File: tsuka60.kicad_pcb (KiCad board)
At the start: 2 copper layers, 285 x 95.1 mm, 175 parts, among them SW1 SW_Push, U1 ATmega32U4-AU, Y1 Resonator_Small

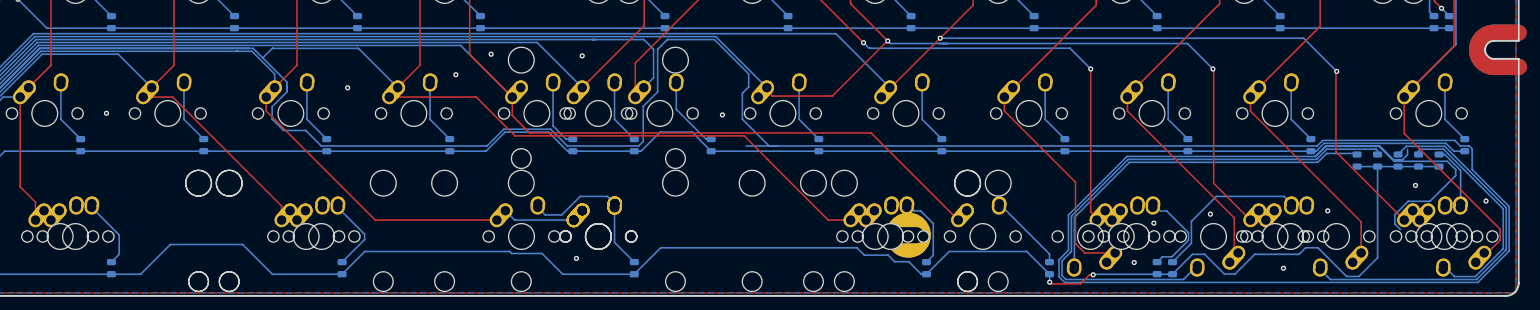
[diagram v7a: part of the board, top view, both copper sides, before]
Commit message: fixed broken trace
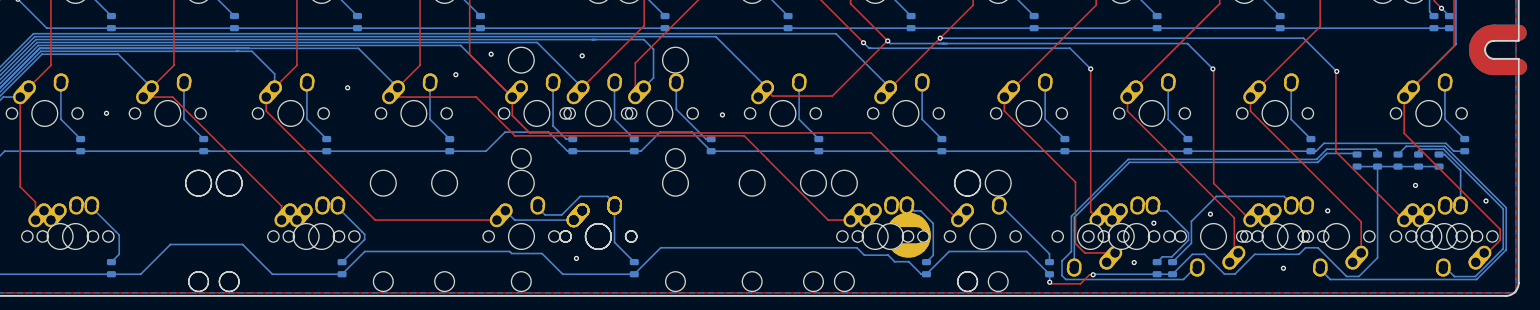
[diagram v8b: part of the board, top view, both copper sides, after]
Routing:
- net Col5: track 759.1 -> 325.0 mm
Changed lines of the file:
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@@
     (thickness 1.6)
     (drawings 1)
-    (tracks 1124)
+    (tracks 1058)
     (zones 0)
     (modules 175)
@@
   (segment (start 209.70875 171.14125) (end 206.25625 174.59375) (width 0.254) (layer F.Cu) (net 84))
   (segment (start 209.70875 157.00375) (end 209.70875 171.14125) (width 0.254) (layer F.Cu) (net 84))
-  (segment (start 139.745453 187.52206) (end 141.40956 185.857953) (width 0.254) (layer B.Cu) (net 84))
-  (segment (start 127.081547 187.52206) (end 139.745453 187.52206) (width 0.254) (layer B.Cu) (net 84))
-  (segment (start 141.40956 185.857953) (end 141.40956 177.90377) (width 0.254) (layer B.Cu) (net 84))
-  (segment (start 141.40956 177.90377) (end 150.80028 168.51305) (width 0.254) (layer B.Cu) (net 84))
-  (segment (start 200.17555 168.51305) (end 206.25625 174.59375) (width 0.254) (layer B.Cu) (net 84))
   (segment (start 224.417548 182.06401) (end 218.407288 176.05375) (width 0.254) (layer F.Cu) (net 84))
   (segment (start 259.91501 182.06401) (end 224.417548 182.06401) (width 0.254) (layer F.Cu) (net 84))
@@
   (segment (start 139.745454 187.52206) (end 141.40956 185.857954) (width 0.254) (layer B.Cu) (net 84))
   (segment (start 118.123 177.94) (end 118.123 180.734) (width 0.254) (layer B.Cu) (net 84))
-  (segment (start 189.103 175.006) (end 189.103 173.736) (width 0.254) (layer B.Cu) (net 84))
-  (segment (start 189.103 174.341538) (end 189.103 175.006) (width 0.254) (layer B.Cu) (net 84))
-  (segment (start 150.80028 168.51305) (end 183.88005 168.51305) (width 0.254) (layer B.Cu) (net 84))
-  (segment (start 186.95995 168.51305) (end 186.83295 168.51305) (width 0.254) (layer B.Cu) (net 84))
-  (segment (start 185.3565 169.9895) (end 183.88005 168.51305) (width 0.254) (layer B.Cu) (net 84))
-  (segment (start 186.83295 168.51305) (end 185.3565 169.9895) (width 0.254) (layer B.Cu) (net 84))
-  (segment (start 189.103 173.736) (end 185.3565 169.9895) (width 0.254) (layer B.Cu) (net 84))
-  (segment (start 186.95995 168.51305) (end 200.17555 168.51305) (width 0.254) (layer B.Cu) (net 84))
-  (segment (start 264.94101 183.62299) (end 260.20399 183.62299) (width 0.254) (layer B.Cu) (net 84))
-  (segment (start 349.931948 183.67523) (end 348.355168 185.25201) (width 0.254) (layer B.Cu) (net 84))
-  (segment (start 358.380552 183.67523) (end 349.931948 183.67523) (width 0.254) (layer B.Cu) (net 84))
-  (segment (start 360.463582 185.75826) (end 358.380552 183.67523) (width 0.254) (layer B.Cu) (net 84))
-  (segment (start 361.848918 185.75826) (end 360.463582 185.75826) (width 0.254) (layer B.Cu) (net 84))
-  (segment (start 362.612826 184.994352) (end 361.848918 185.75826) (width 0.254) (layer B.Cu) (net 84))
-  (segment (start 362.612826 184.12924) (end 362.612826 184.994352) (width 0.254) (layer B.Cu) (net 84))
-  (segment (start 369.926552 182.76721) (end 349.490723 182.76721) (width 0.254) (layer B.Cu) (net 84))
-  (segment (start 348.634943 183.62299) (end 264.94101 183.62299) (width 0.254) (layer B.Cu) (net 84))
-  (segment (start 372.167668 183.62299) (end 370.782332 183.62299) (width 0.254) (layer B.Cu) (net 84))
-  (segment (start 372.618 184.073322) (end 372.167668 183.62299) (width 0.254) (layer B.Cu) (net 84))
-  (segment (start 372.618 187.264188) (end 372.618 184.073322) (width 0.254) (layer B.Cu) (net 84))
-  (segment (start 373.501327 204.756769) (end 378.35202 199.906076) (width 0.254) (layer B.Cu) (net 84))
-  (segment (start 378.35202 192.998208) (end 372.618 187.264188) (width 0.254) (layer B.Cu) (net 84))
-  (segment (start 349.490723 182.76721) (end 348.634943 183.62299) (width 0.254) (layer B.Cu) (net 84))
-  (segment (start 308.66399 201.233943) (end 308.66399 203.896057) (width 0.254) (layer B.Cu) (net 84))
-  (segment (start 309.524702 204.756769) (end 373.501327 204.756769) (width 0.254) (layer B.Cu) (net 84))
-  (segment (start 310.12323 199.774704) (end 308.66399 201.233943) (width 0.254) (layer B.Cu) (net 84))
-  (segment (start 308.66399 203.896057) (end 309.524702 204.756769) (width 0.254) (layer B.Cu) (net 84))
-  (segment (start 310.12323 194.313702) (end 310.12323 199.774704) (width 0.254) (layer B.Cu) (net 84))
-  (segment (start 378.35202 199.906076) (end 378.35202 192.998208) (width 0.254) (layer B.Cu) (net 84))
-  (segment (start 318.91897 185.517964) (end 310.12323 194.313702) (width 0.254) (layer B.Cu) (net 84))
-  (segment (start 370.782332 183.62299) (end 369.926552 182.76721) (width 0.254) (layer B.Cu) (net 84))
-  (segment (start 319.184923 185.25201) (end 318.91897 185.517964) (width 0.254) (layer B.Cu) (net 84))
-  (segment (start 348.355168 185.25201) (end 319.184923 185.25201) (width 0.254) (layer B.Cu) (net 84))
-  (segment (start 360.657359 194.256179) (end 360.657359 195.703485) (width 0.254) (layer B.Cu) (net 84))
-  (segment (start 366.100251 192.191749) (end 362.721789 192.191749) (width 0.254) (layer B.Cu) (net 84))
-  (segment (start 370.078 188.214) (end 366.100251 192.191749) (width 0.254) (layer B.Cu) (net 84))
-  (segment (start 370.078 187.292454) (end 370.078 188.214) (width 0.254) (layer B.Cu) (net 84))
-  (segment (start 360.657359 195.703485) (end 361.509015 196.555141) (width 0.254) (layer B.Cu) (net 84))
-  (segment (start 362.721789 192.191749) (end 360.657359 194.256179) (width 0.254) (layer B.Cu) (net 84))
-  (segment (start 368.789786 186.00424) (end 370.078 187.292454) (width 0.254) (layer B.Cu) (net 84))
-  (segment (start 348.355168 185.25201) (end 349.931947 183.67523) (width 0.254) (layer B.Cu) (net 84))
-  (segment (start 360.548918 186.00424) (end 368.789786 186.00424) (width 0.254) (layer B.Cu) (net 84))
-  (segment (start 358.219908 183.67523) (end 360.548918 186.00424) (width 0.254) (layer B.Cu) (net 84))
-  (segment (start 349.931947 183.67523) (end 358.219908 183.67523) (width 0.254) (layer B.Cu) (net 84))
-  (segment (start 188.595 181.229) (end 186.817 179.451) (width 0.254) (layer B.Cu) (net 84))
-  (segment (start 194.41799 183.62299) (end 192.024 181.229) (width 0.254) (layer B.Cu) (net 84))
-  (segment (start 229.92399 181.02899) (end 222.696943 181.02899) (width 0.254) (layer B.Cu) (net 84))
-  (segment (start 243.580168 183.62299) (end 232.51799 183.62299) (width 0.254) (layer B.Cu) (net 84))
-  (segment (start 186.817 177.546) (end 189.103 175.26) (width 0.254) (layer B.Cu) (net 84))
-  (segment (start 244.272079 182.931079) (end 243.580168 183.62299) (width 0.254) (layer B.Cu) (net 84))
-  (segment (start 186.817 179.451) (end 186.817 177.546) (width 0.254) (layer B.Cu) (net 84))
-  (segment (start 192.024 181.229) (end 188.595 181.229) (width 0.254) (layer B.Cu) (net 84))
-  (segment (start 244.272079 177.494921) (end 244.272079 182.931079) (width 0.254) (layer B.Cu) (net 84))
-  (segment (start 189.103 175.26) (end 189.103 175.006) (width 0.254) (layer B.Cu) (net 84))
-  (segment (start 246.507 175.26) (end 244.272079 177.494921) (width 0.254) (layer B.Cu) (net 84))
-  (segment (start 222.696943 181.02899) (end 220.102943 183.62299) (width 0.254) (layer B.Cu) (net 84))
-  (segment (start 232.51799 183.62299) (end 229.92399 181.02899) (width 0.254) (layer B.Cu) (net 84))
-  (segment (start 246.507 168.656) (end 246.507 175.26) (width 0.254) (layer B.Cu) (net 84))
-  (segment (start 248.01198 167.15102) (end 246.507 168.656) (width 0.254) (layer B.Cu) (net 84))
-  (segment (start 255.28902 167.15102) (end 248.01198 167.15102) (width 0.254) (layer B.Cu) (net 84))
-  (segment (start 260.604 172.466) (end 255.28902 167.15102) (width 0.254) (layer B.Cu) (net 84))
-  (segment (start 260.604 174.498) (end 260.604 172.466) (width 0.254) (layer B.Cu) (net 84))
-  (segment (start 259.624249 175.477751) (end 260.604 174.498) (width 0.254) (layer B.Cu) (net 84))
-  (segment (start 220.102943 183.62299) (end 194.41799 183.62299) (width 0.254) (layer B.Cu) (net 84))
-  (segment (start 263.760358 183.62299) (end 259.624249 179.486881) (width 0.254) (layer B.Cu) (net 84))
-  (segment (start 259.624249 179.486881) (end 259.624249 175.477751) (width 0.254) (layer B.Cu) (net 84))
-  (segment (start 264.94101 183.62299) (end 263.760358 183.62299) (width 0.254) (layer B.Cu) (net 84))
+  (segment (start 200.17555 168.51305) (end 206.25625 174.59375) (width 0.254) (layer B.Cu) (net 84))
+  (segment (start 141.40956 185.857953) (end 141.40956 177.90377) (width 0.254) (layer B.Cu) (net 84))
+  (segment (start 139.745453 187.52206) (end 141.40956 185.857953) (width 0.254) (layer B.Cu) (net 84))
+  (segment (start 127.081547 187.52206) (end 139.745453 187.52206) (width 0.254) (layer B.Cu) (net 84))
+  (segment (start 150.80028 168.51305) (end 200.17555 168.51305) (width 0.254) (layer B.Cu) (net 84))
+  (segment (start 141.40956 177.90377) (end 150.80028 168.51305) (width 0.254) (layer B.Cu) (net 84))
   (segment (start 214.47125 135.18375) (end 215.78125 136.49375) (width 0.254) (layer F.Cu) (net 85))
   (segment (start 214.47125 118.90375) (end 214.47125 135.18375) (width 0.254) (layer F.Cu) (net 85))
